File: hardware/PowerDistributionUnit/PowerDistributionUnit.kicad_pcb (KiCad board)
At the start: 2 copper layers, 101 parts, among them J1 973582101, J2 973582100, J3 973582101, J4 973582100, Q1 SQJ141ELP, Q2 CSD18511Q5A, SW1 SW_Push, U1 TPS25983, U2 AD5258, U3 NUCLEO_LK43C

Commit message: started layout
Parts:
- C1, C2, R1, R2, R4, R5, R50, R6: moved to B.Cu
- moved R1 96.1 mm to (93.6, 129.0), turned to 180 degrees
- moved R2 95.2 mm to (93.6, 131.1), turned to 180 degrees
- moved TP5 94.7 mm to (63.8, 130.6)
- moved J4 92.5 mm to (141.6, 116.5), turned to 180 degrees
- moved R57 91.6 mm to (84.0, 128.3)
- moved J3 88.5 mm to (141.6, 97.5), turned to 180 degrees
- moved R58 87.9 mm to (87.6, 128.3)
- moved R4 87.9 mm to (86.0, 129.2)
- moved R5 84.6 mm to (89.6, 129.2), turned to 180 degrees
- moved R59 84.4 mm to (91.3, 128.3)
- moved JP14 84.2 mm to (141.7, 127.9)
- moved TP8 78.5 mm to (140.5, 108.6)
- moved R50 78.0 mm to (95.1, 113.4), turned to 180 degrees
- moved JP15 76.8 mm to (138.0, 127.9)
- moved R7 76.2 mm to (72.0, 104.1)
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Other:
- board text added: "(V/ms)"
- board text added: "(ns)"
- board text added: "0.2"
- board text added: "0.5"
- board text added: "1"
- board text added: "1.5"
- board text added: "12A"
- board text added: "16"
- board text added: "2A"
- board text added: "5A"
- board text added: "9.3"
- board text added: "91.7"
- board text added: "915"
- board text added: "AD0"
- board text added: "AD1"
- board text added: "C9"
- board text added: "I2C ADR"
- board text added: "ILIM"
- board text added: "MI6 colonization"
- board text added: "NRETRY"
- board text added: "PRG"
- board text added: "RETRY_DLY"
- board text added: "SLEW RATE"
- board text added: "∞"

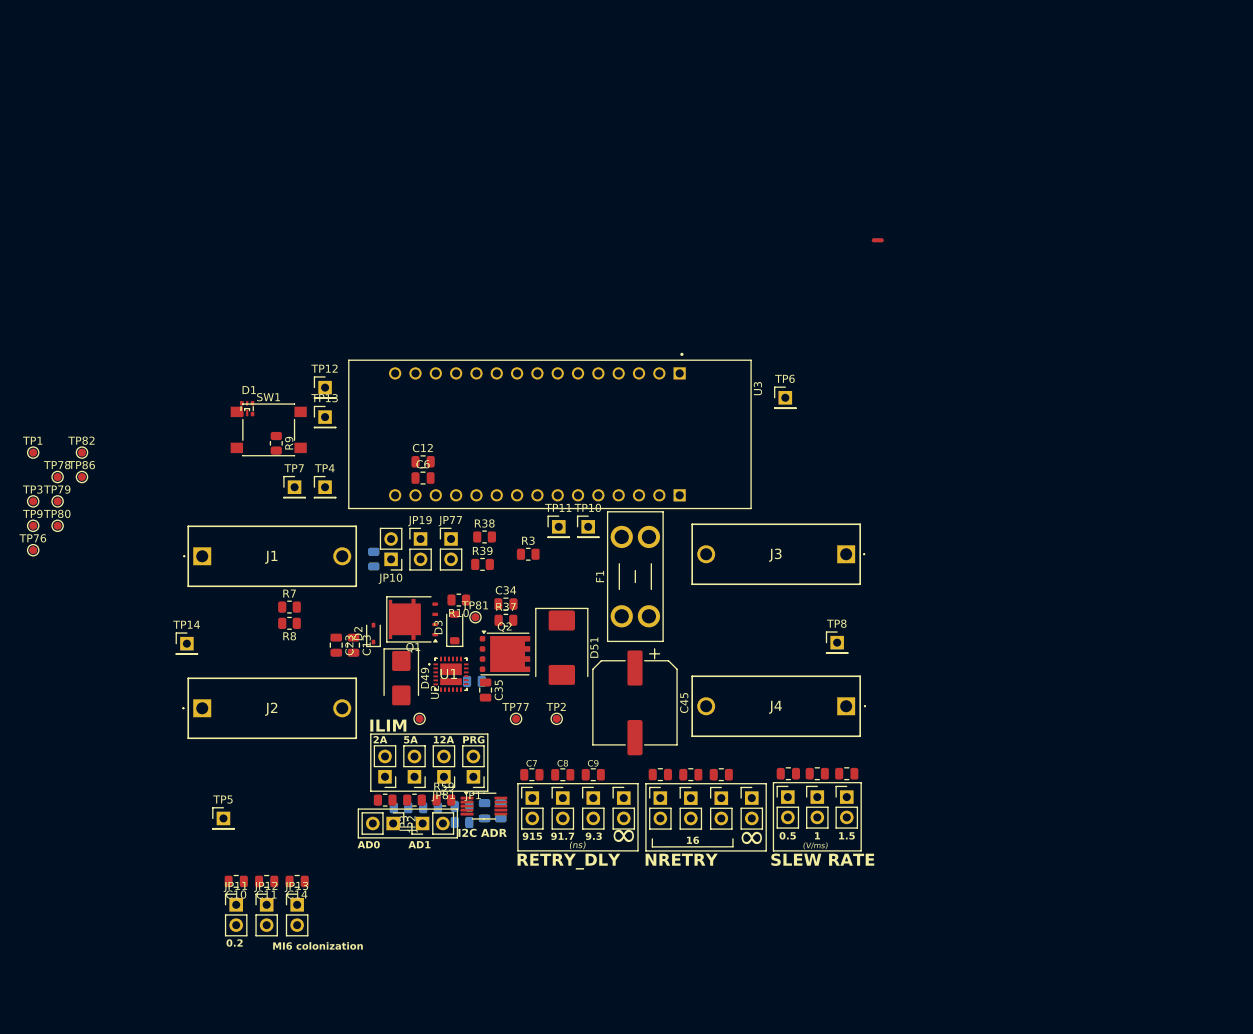
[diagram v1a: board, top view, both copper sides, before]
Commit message: Finished placing components for layout, began traces
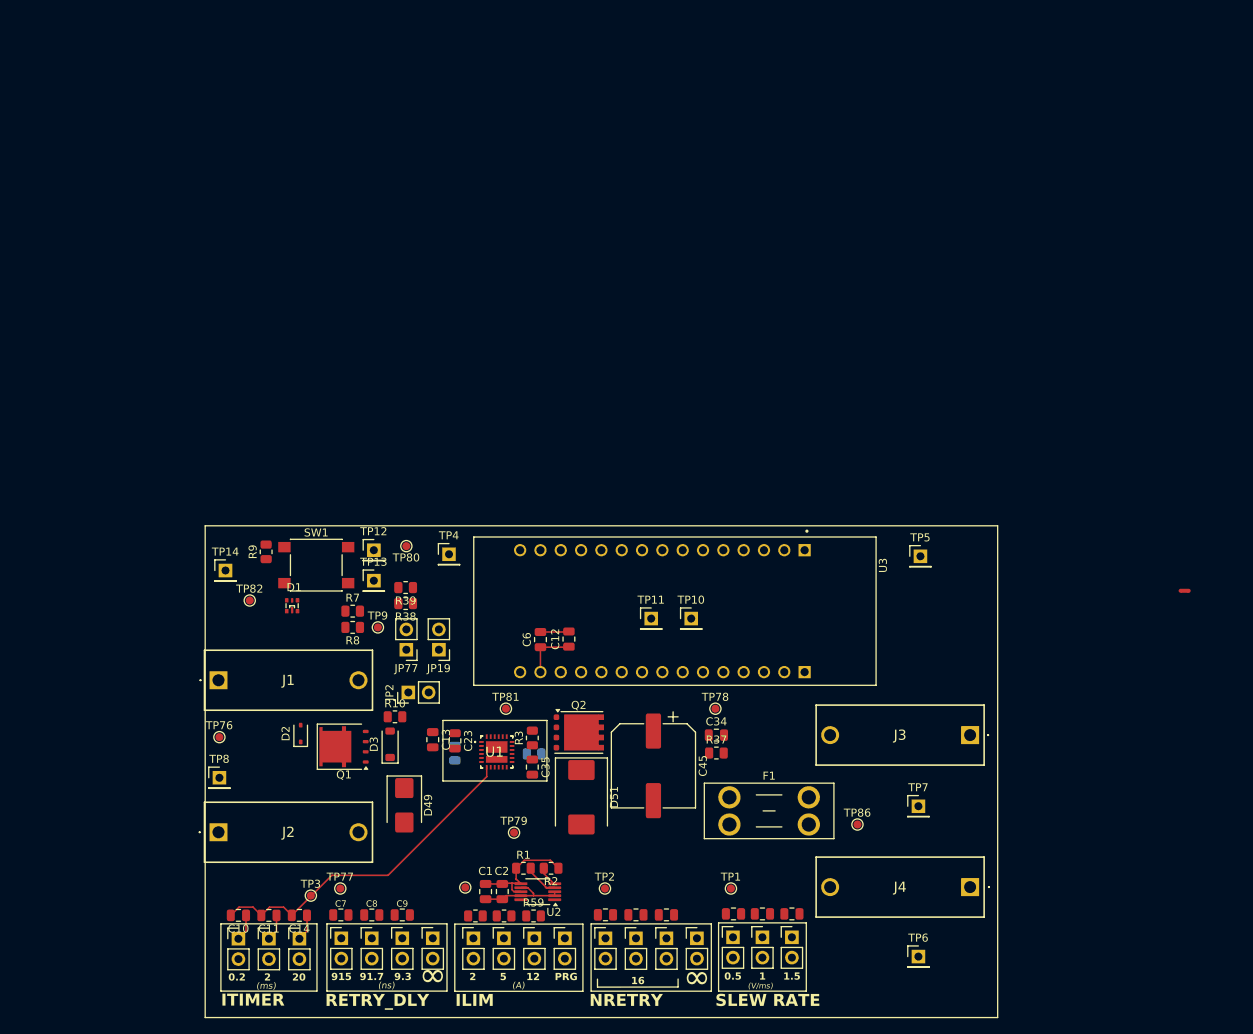
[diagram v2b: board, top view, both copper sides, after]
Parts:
- removed JP10: JP, Connector_PinHeader_2.54mm:PinHeader_1x02_P2.54mm_Vertical
- removed JP3: Jumper_2_Small_Open, Connector_PinHeader_2.54mm:PinHeader_1x02_P2.54mm_Vertical
- removed R4, R5: 1k, Resistor_SMD:R_0805_2012Metric
- C1, C2, R1, R2: moved to F.Cu
- U3: value NUCLEO_LK43C -> NUCLEO_L432KC
- moved TP86 106.2 mm to (143.0, 131.3)
- moved TP1 102.8 mm to (127.2, 139.3)
- moved TP5 93.1 mm to (150.9, 97.8)
- moved TP7 87.6 mm to (150.6, 129.0)
- moved TP78 87.2 mm to (125.2, 116.8)
- moved TP8 79.0 mm to (63.2, 125.5)
- moved TP6 71.8 mm to (150.6, 147.8)
- moved TP79 70.5 mm to (100.1, 132.3)
- moved TP3 60.3 mm to (74.7, 140.2)
- moved NT1 58.2 mm to (183.9, 102.1)
- moved TP9 44.9 mm to (83.1, 106.7)
- moved TP80 43.7 mm to (86.6, 96.5), turned to 180 degrees
- moved TP76 33.0 mm to (63.2, 120.4)
- moved R37 31.1 mm to (125.4, 122.4)
- moved C34 31.0 mm to (125.4, 120.1)
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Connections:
- C10 pad 2: GND -> /ITIMER
- C11 pad 2: GND -> /ITIMER
- C14 pad 2: GND -> /ITIMER
- C15 pad 2: GND -> /dVdt/BGATE
- C16 pad 2: GND -> /dVdt/BGATE
- C17 pad 2: GND -> /dVdt/BGATE
- C3 pad 2: GND -> /NRETRY
- C4 pad 2: GND -> /NRETRY
- C5 pad 2: GND -> /NRETRY
- C7 pad 2: GND -> /RETRY_DLY
- C8 pad 2: GND -> /RETRY_DLY
- C9 pad 2: GND -> /RETRY_DLY
- JP11 pad 2: /ITIMER -> GND
- JP12 pad 2: /ITIMER -> GND
- JP13 pad 2: /ITIMER -> GND
- JP14 pad 2: /dVdt/BGATE -> GND
- JP15 pad 2: /dVdt/BGATE -> GND
- JP16 pad 2: /dVdt/BGATE -> GND
- JP19 pad 2: /EN_PIN -> +3V3
- JP2 pad 1: /ILIM_AD0 -> /IN
- JP2 pad 2: +3V3 -> /EFUSE_IN
- JP4 pad 2: /NRETRY -> GND
- JP5 pad 2: /NRETRY -> GND
- JP6 pad 2: /NRETRY -> GND
- JP7 pad 2: /RETRY_DLY -> GND
- JP79 pad 2: /ILIM -> GND
- JP8 pad 2: /RETRY_DLY -> GND
- JP80 pad 2: /ILIM -> GND
- JP81 pad 2: /ILIM -> GND
- JP9 pad 2: /RETRY_DLY -> GND
- R57 pad 2: GND -> /ILIM
- R58 pad 2: GND -> /ILIM
- R59 pad 2: GND -> /ILIM
- R6 pad 1: /EN_PIN -> +3V3
- TP82 pad 1: /EN_PIN -> +3V3
- U1 pad 6: /EN_PIN -> +3V3
- U2 pad 2: /ILIM_AD0 -> GND
- U2 pad 3: /ILIM_AD1 -> GND
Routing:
- net /ITIMER: track 0.00 -> 42.0 mm
- net +3V3: track 0.00 -> 21.6 mm
- net GND: track 0.00 -> 15.6 mm
- net /ILIM_SDA: track 0.00 -> 5.43 mm
- net Net-(JP13-A): track 0.00 -> 3.32 mm
- net Net-(JP11-A): track 0.00 -> 3.32 mm
- net Net-(JP12-A): track 0.00 -> 3.31 mm
- net /ILIM_SCL: track 0.00 -> 2.60 mm
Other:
- board text added: "(A)"
- board text added: "(ms)"
- board text added: "12"
- board text added: "2"
- board text added: "20"
- board text added: "5"
- board text added: "ITIMER"
- board text removed: "12A"
- board text removed: "2A"
- board text removed: "5A"
- board text removed: "AD0"
- board text removed: "AD1"
- board text removed: "I2C ADR"
- board text removed: "MI6 colonization"

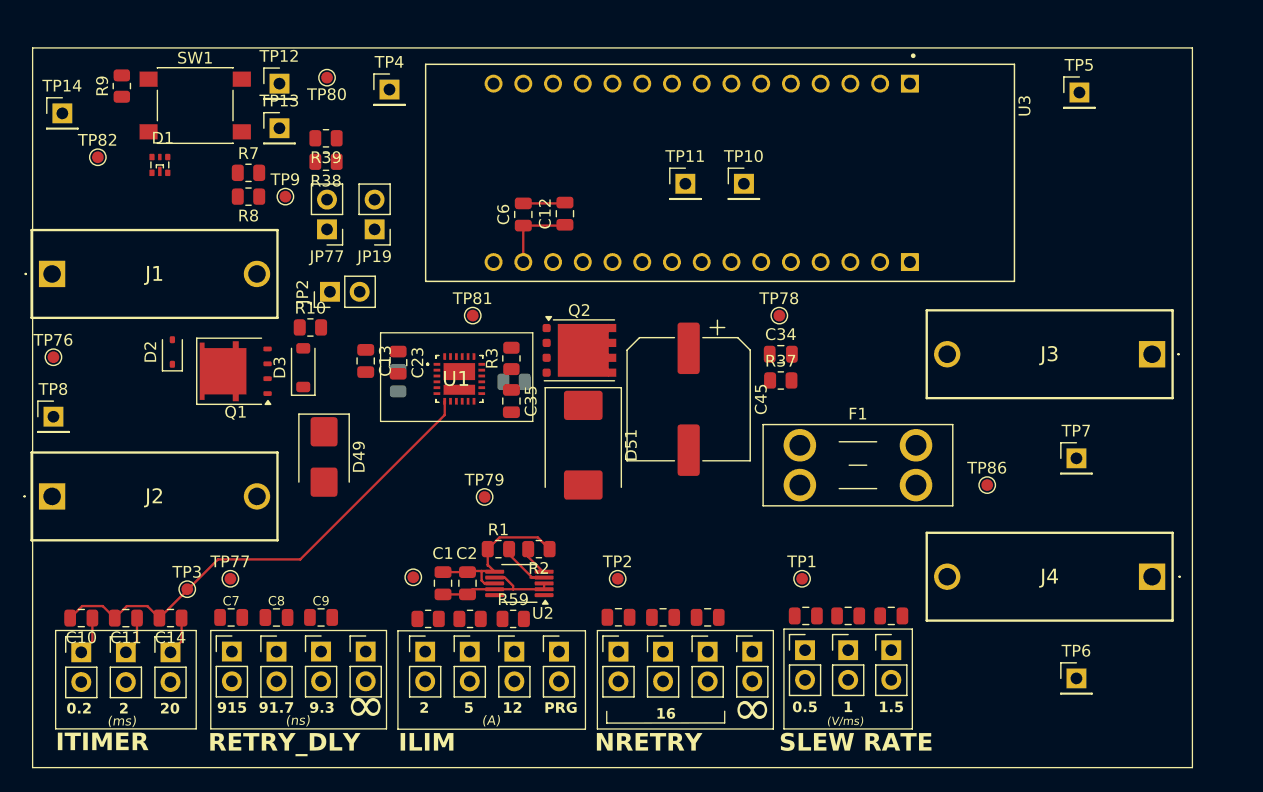
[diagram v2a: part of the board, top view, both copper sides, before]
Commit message: modified layout, corrected en circuit, corrected uvlo labeling from disable to enable, changed more test points to gndpwr from gnd, started making some labels
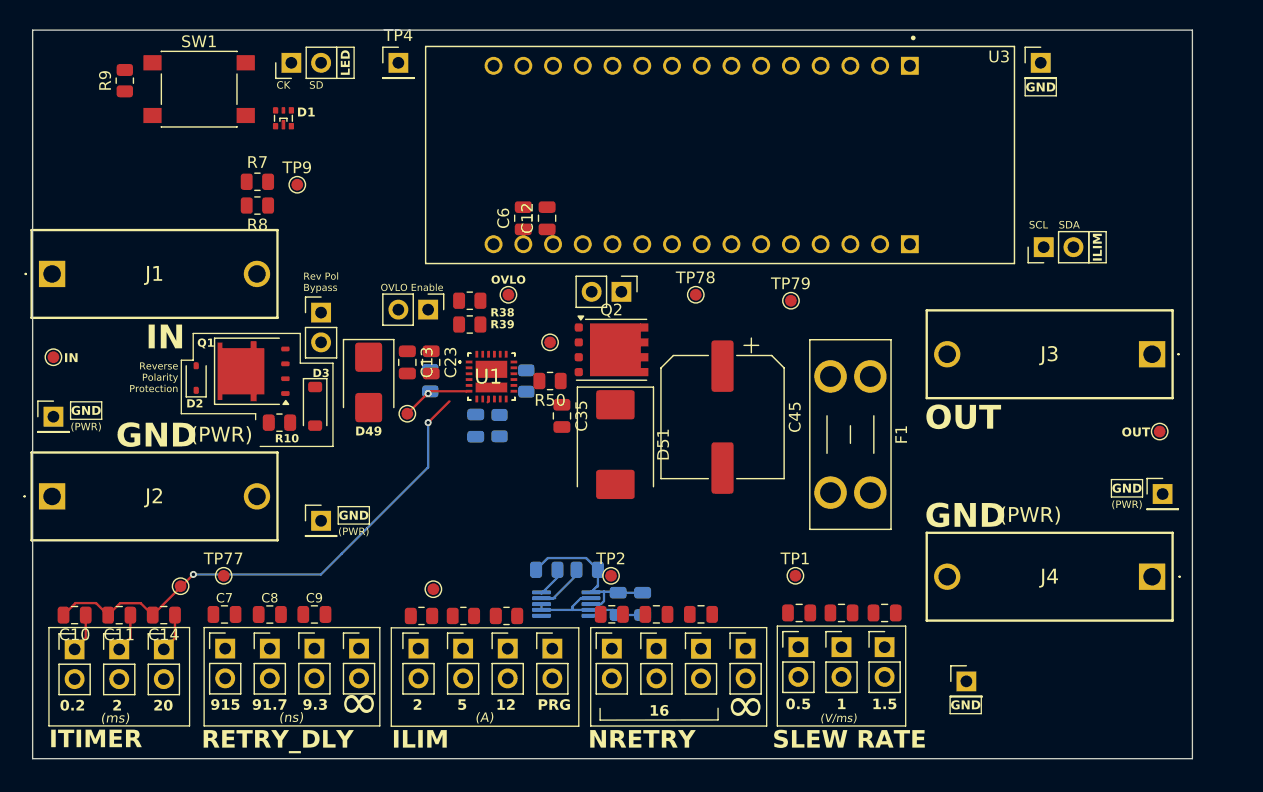
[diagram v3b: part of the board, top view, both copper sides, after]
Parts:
- removed TP12: LED_CK, Connector_PinHeader_2.54mm:PinHeader_1x01_P2.54mm_Vertical
- removed TP13: LED_SD, Connector_PinHeader_2.54mm:PinHeader_1x01_P2.54mm_Vertical
- C1, C2, C34, R1, R2, R3, R37, U2: moved to B.Cu
- R50: moved to F.Cu
- TP10: value ILIM_SCL -> Conn_01x02; footprint Connector_PinHeader_2.54mm:PinHeader_1x01_P2.54mm_Vertical -> Connector_PinHeader_2.54mm:PinHeader_1x02_P2.54mm_Vertical
- TP11: value ILIM_SDA -> Conn_01x02; footprint Connector_PinHeader_2.54mm:PinHeader_1x01_P2.54mm_Vertical -> Connector_PinHeader_2.54mm:PinHeader_1x02_P2.54mm_Vertical
- moved TP14 41.2 mm to (86.1, 134.4)
- moved TP10 40.0 mm to (83.6, 95.2), turned to 90 degrees
- moved TP82 34.3 mm to (93.5, 125.2)
- moved TP11 31.1 mm to (147.8, 111.0), turned to 90 degrees
- moved TP79 31.1 mm to (126.2, 115.6)
- moved C34 26.8 mm to (99.3, 126.2), turned to -90 degrees
- moved R37 24.3 mm to (101.3, 126.2), turned to -90 degrees
- moved TP80 24.2 mm to (102.1, 115.1)
- moved JP19 21.7 mm to (111.8, 114.8), turned to -90 degrees
- moved R39 20.1 mm to (98.8, 117.6), turned to 0 degrees
- moved C1 17.1 mm to (113.6, 141.5)
- moved R38 17.1 mm to (98.8, 115.6), turned to 0 degrees
- moved TP86 15.4 mm to (157.7, 126.7)
- moved C2 13.0 mm to (111.5, 141.5)
- moved D1 11.3 mm to (82.9, 100.0)
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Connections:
- JP19 pad 2: +3V3 -> /EN_PIN
- R6 pad 1: +3V3 -> /EN_PIN
- R6 pad 2: GND -> +3V3
- R8 pad 2: GND -> GNDPWR
- TP10 pad 1: /ILIM_SCL -> /LED_CK
- TP11 pad 1: /ILIM_SDA -> /ILIM_SCL
- TP7 pad 1: GND -> GNDPWR
- TP8 pad 1: GND -> GNDPWR
- TP82 pad 1: +3V3 -> /EN_PIN
- U1 pad 6: +3V3 -> /EN_PIN
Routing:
- net +3V3: track 21.6 -> 15.0 mm
- net /EN_PIN: track 0.00 -> 5.87 mm, vias 0 -> 1
- net GND: track 15.6 -> 12.0 mm
- net /ITIMER: track 42.0 -> 44.5 mm, vias 0 -> 2
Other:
- board outline added: 99.1 x 62.2 mm
- board text added: "(PWR)"
- board text added: "CK"
- board text added: "GND"
- board text added: "IN"
- board text added: "LED"
- board text added: "OUT"
- board text added: "OVLO"
- board text added: "OVLO Enable"
- board text added: "Rev Pol Bypass"
- board text added: "Reverse Polarity Protection"
- board text added: "SCL"
- board text added: "SD"
- board text added: "SDA"
